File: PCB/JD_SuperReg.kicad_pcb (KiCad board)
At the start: 2 copper layers, 190.5 x 152.4 mm, 130 parts, among them J1 Conn_01x02_Male, J2 Conn_01x03_Male, J3 Conn_01x03_Male, J4 Conn_01x02_Male, Q101 D44H11, Q102 BC556, Q103 D45H11, Q104 BC546, Q201 D44H11, Q202 BC556, Q203 D45H11, Q204 BC546, T1 18V + 18V, T2 18V + 18V, U101 AD825ARZ, U102 AD825ARZ, U201 AD825ARZ, U202 AD825ARZ

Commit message: Finalized layout
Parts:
- removed C101, C102, C103, C104, C105, C106, C107, C108, C109, C110, C201, C202, C203, C204, C205, C206, C207, C208, C209, C210: 120uF, Capacitor_THT:CP_Radial_D10.0mm_P5.00mm
- removed C111, C112, C211, C212: 100pF, Capacitor_THT:C_Disc_D4.7mm_W2.5mm_P5.00mm
- removed C15, C16: 2200uF, Capacitor_THT:CP_Radial_D18.0mm_P7.50mm
- removed D101, D106, D201, D206: LED, LED_THT:LED_D3.0mm
- removed D102, D107, D202, D207: D_Zener, Diode_THT:D_DO-35_SOD27_P10.16mm_Horizontal
- removed D103, D104, D108, D109, D203, D204, D208, D209: D, Diode_THT:D_DO-35_SOD27_P10.16mm_Horizontal
- removed D105, D110, D205, D210: LM329, Package_TO_SOT_THT:TO-92_Inline
- removed F3, F4: Fuse, HP_Footprints:5x20mm-BK-1A3399-01-fuseholder
- removed HS101, HS102, HS201, HS202: Heatsink, Heatsink:Heatsink_Fischer_SK104-STCB_35x13mm__2xDrill3.5mm_ScrewM3
- removed Q101, Q201: D44H11, Package_TO_SOT_THT:TO-220-3_Vertical
- removed Q102, Q202: BC556, Package_TO_SOT_THT:TO-92_Inline
- removed Q103, Q203: D45H11, Package_TO_SOT_THT:TO-220-3_Vertical
- removed Q104, Q204: BC546, Package_TO_SOT_THT:TO-92_Inline
- removed R101, R108, R201, R208: 249R, Resistor_THT:R_Axial_DIN0207_L6.3mm_D2.5mm_P10.16mm_Horizontal
- removed R102, R109, R202, R209: 10K, Resistor_THT:R_Axial_DIN0207_L6.3mm_D2.5mm_P10.16mm_Horizontal
- removed R103, R110, R203, R210: 10R, Resistor_THT:R_Axial_DIN0207_L6.3mm_D2.5mm_P10.16mm_Horizontal
- removed R104, R111, R204, R211: 499R, Resistor_THT:R_Axial_DIN0207_L6.3mm_D2.5mm_P10.16mm_Horizontal
- removed R105, R112, R205, R212: 4.99K, Resistor_THT:R_Axial_DIN0207_L6.3mm_D2.5mm_P10.16mm_Horizontal
- removed R106, R107, R113, R114, R206, R207, R213, R214: 1K, Resistor_THT:R_Axial_DIN0207_L6.3mm_D2.5mm_P10.16mm_Horizontal
- removed R115, R116, R216: 100R, Resistor_THT:R_Axial_DIN0207_L6.3mm_D2.5mm_P10.16mm_Horizontal
- removed R215: 100, Resistor_THT:R_Axial_DIN0207_L6.3mm_D2.5mm_P10.16mm_Horizontal
- removed T1, T2: 18V + 18V, Super-Regulator Combined Dual:Talema-25VA-Transformer
- removed U101, U102, U201, U202: AD825ARZ, Package_SO:SOIC-8_3.9x4.9mm_P1.27mm
- added D10: 9V1, Diode_SMD:D_SOD-123, F.Cu at (105.9, 73.5)
- added D11: 4148, Diode_SMD:D_SOD-123, F.Cu at (113.4, 57.0)
- added D12: 4148, Diode_SMD:D_SOD-123, F.Cu at (113.4, 63.6)
- added D13: 4148, Diode_SMD:D_SOD-123, F.Cu at (113.4, 59.4)
- added D14: 4148, Diode_SMD:D_SOD-123, F.Cu at (113.4, 66.0)
- added D15: 9V1, Diode_SMD:D_SOD-123, F.Cu at (130.4, 56.2)
- added D16: 9V1, Diode_SMD:D_SOD-123, F.Cu at (132.8, 56.2)
- added D17: 9V1, Diode_SMD:D_SOD-123, F.Cu at (132.8, 66.8)
- added D18: 9V1, Diode_SMD:D_SOD-123, F.Cu at (130.4, 66.8)
- added D9: 9V1, Diode_SMD:D_SOD-123, F.Cu at (105.9, 49.6)
- added G***: LOGO, Ariamelon-Logo:Ariamelon_Logo_Medium_Mask, B.Cu at (143.6, 61.5)
- added H1: M3, Ariamelon-HolePad:MountingHole_3.2mm_M3_Pad, F.Cu at (59.0, 31.5)
- added H2: M3, Ariamelon-HolePad:MountingHole_3.2mm_M3_Pad, F.Cu at (59.0, 91.5)
- added H3: M3, Ariamelon-HolePad:MountingHole_3.2mm_M3_Pad, F.Cu at (149.0, 31.5)
- added H4: M3, Ariamelon-HolePad:MountingHole_3.2mm_M3_Pad, F.Cu at (149.0, 91.5)
- added HS1: Heatsink, Ariamelon-Misc:Heatsink, F.Cu at (117.5, 88.1)
- added HS2: Heatsink, Ariamelon-Misc:Heatsink, F.Cu at (117.5, 34.9)
- added J5: V-_Jumper, Ariamelon-Header:PinHeader_1x04_P2.54mm_Vertical_Jumper, F.Cu at (139.6, 72.9)
- added Q1: BCM857DS, Ariamelon-Package:SOT-23-6, F.Cu at (108.2, 44.5)
- added Q10: BCM847DS, Ariamelon-Package:SOT-23-6, F.Cu at (131.6, 73.4)
- added Q2: BCM847DS, Ariamelon-Package:SOT-23-6, F.Cu at (108.2, 78.5)
- added Q3: D44H11, Ariamelon-Package:TO-220-3_TO-247_Combined_Vertical, F.Cu at (117.5, 38.7)
- added Q4: D45H11, Ariamelon-Package:TO-220-3_TO-247_Combined_Vertical, F.Cu at (117.5, 84.3)
- added Q5: ZXTP2041F, Ariamelon-Package:SOT-23-3, F.Cu at (108.9, 50.4)
- added Q6: ZXTN2040F, Ariamelon-Package:SOT-23-3, F.Cu at (108.9, 72.6)
- added Q9: BCM857DS, Ariamelon-Package:SOT-23-6, F.Cu at (131.6, 49.6)
- added R11: 100, Resistor_SMD:R_MiniMELF_MMA-0204, F.Cu at (131.6, 52.6)
- added R12: 120, Resistor_SMD:R_MiniMELF_MMA-0204, F.Cu at (131.6, 70.4)
- added R13: 10K, Resistor_SMD:R_MiniMELF_MMA-0204, F.Cu at (135.4, 52.6)
- added R14: 10K, Resistor_SMD:R_MiniMELF_MMA-0204, F.Cu at (135.4, 70.4)
- added R15: 1k2, Resistor_SMD:R_MiniMELF_MMA-0204, F.Cu at (126.2, 48.8)
- added R16: 1k5, Resistor_SMD:R_MiniMELF_MMA-0204, F.Cu at (126.2, 56.4)
- added R17: 1k5, Resistor_SMD:R_MiniMELF_MMA-0204, F.Cu at (126.2, 66.6)
- added R18: 1k2, Resistor_SMD:R_MiniMELF_MMA-0204, F.Cu at (126.2, 74.2)
- added R5: 120, Resistor_SMD:R_MiniMELF_MMA-0204, F.Cu at (105.2, 44.4)
- added R6: 100, Resistor_SMD:R_MiniMELF_MMA-0204, F.Cu at (105.2, 78.5)
- added R7: 4k7, Resistor_SMD:R_MiniMELF_MMA-0204, F.Cu at (126.2, 52.6)
- added R8: 4k7, Resistor_SMD:R_MiniMELF_MMA-0204, F.Cu at (126.2, 70.4)
- added U1: ADA4522, Ariamelon-Package:SOIC-8_3.9x4.9mm_P1.27mm, F.Cu at (113.4, 52.0)
- added U2: ADA4522, Ariamelon-Package:SOIC-8_3.9x4.9mm_P1.27mm, F.Cu at (113.4, 71.0)
- C1: value 0.15uF -> 100n; footprint Capacitor_THT:C_Rect_L7.2mm_W3.5mm_P5.00mm_FKS2_FKP2_MKS2_MKP2 -> Ariamelon-Device:C_1206_3216Metric
- C10, C11: value 0.01uF -> 150u; footprint Capacitor_THT:C_Rect_L7.2mm_W2.5mm_P5.00mm_FKS2_FKP2_MKS2_MKP2 -> Capacitor_THT:CP_Radial_D8.0mm_P3.50mm
- C12, C13, C5, C7, C8: value 2200uF -> 150u; footprint Capacitor_THT:CP_Radial_D18.0mm_P7.50mm -> Capacitor_THT:CP_Radial_D8.0mm_P3.50mm
- C14, C6, C9: value 0.15uF -> 150u; footprint Capacitor_THT:C_Rect_L7.2mm_W3.5mm_P5.00mm_FKS2_FKP2_MKS2_MKP2 -> Capacitor_THT:CP_Radial_D8.0mm_P3.50mm
- C2: value 0.01uF -> 100n; footprint Capacitor_THT:C_Rect_L7.2mm_W2.5mm_P5.00mm_FKS2_FKP2_MKS2_MKP2 -> Ariamelon-Device:C_1206_3216Metric
- C3: value 0.01uF -> 4700u; footprint Capacitor_THT:C_Rect_L7.2mm_W2.5mm_P5.00mm_FKS2_FKP2_MKS2_MKP2 -> Capacitor_THT:CP_Radial_D18.0mm_P7.50mm
- C4: value 2200uF -> 4700u
- D1: value SB180 -> SBYV27; footprint Diode_THT:D_DO-41_SOD81_P10.16mm_Horizontal -> Diode_THT:D_DO-15_P10.16mm_Horizontal
- D2, D3, D4, D5, D6, D7, D8: value D -> SBYV27; footprint Diode_THT:D_DO-41_SOD81_P10.16mm_Horizontal -> Diode_THT:D_DO-15_P10.16mm_Horizontal
- F1, F2: value Fuse -> Fuse_Small; footprint HP_Footprints:5x20mm-BK-1A3399-01-fuseholder -> Fuse:Fuseholder_Cylinder-5x20mm_Schurter_0031_8201_Horizontal_Open
- J1: value Conn_01x02_Male -> V+_In; footprint HP_Footprints:2-pad-wire-connector-22-ga -> TerminalBlock_Phoenix:TerminalBlock_Phoenix_MKDS-1,5-2-5.08_1x02_P5.08mm_Horizontal
- J2: value Conn_01x03_Male -> V-_In; footprint HP_Footprints:3-pad-wire-connector-22-ga -> TerminalBlock_Phoenix:TerminalBlock_Phoenix_MKDS-1,5-2-5.08_1x02_P5.08mm_Horizontal
- J3: value Conn_01x03_Male -> Out; footprint HP_Footprints:3-pad-wire-connector-22-ga -> Ariamelon-Connector:TerminalBlock_Phoenix_MKDS-1,5-8-5.08_1x08_P5.08mm_Horizontal
- J4: value Conn_01x02_Male -> V+_Jumper; footprint HP_Footprints:2-pad-wire-connector-22-ga -> Ariamelon-Header:PinHeader_1x04_P2.54mm_Vertical_Jumper
- R1, R2: value 32R -> 10; footprint Resistor_THT:R_Axial_DIN0207_L6.3mm_D2.5mm_P10.16mm_Horizontal -> Resistor_SMD:R_MiniMELF_MMA-0204
- R3, R4: value 32R -> 10K; footprint Resistor_THT:R_Axial_DIN0207_L6.3mm_D2.5mm_P10.16mm_Horizontal -> Resistor_SMD:R_MiniMELF_MMA-0204
- moved J2 248.9 mm to (60.8, 69.1), turned to -90 degrees
- moved J3 186.1 mm to (147.2, 79.3)
- moved F1 168.3 mm to (64.5, 33.3), turned to 0 degrees
- moved F2 167.5 mm to (64.5, 89.7), turned to 0 degrees
- moved D6 164.1 mm to (70.9, 54.0), turned to 0 degrees
- moved D7 159.2 mm to (81.1, 69.0), turned to 180 degrees
- moved D5 157.7 mm to (70.9, 59.0), turned to 0 degrees
- moved D8 152.4 mm to (81.1, 64.0), turned to 180 degrees
- moved C13 152.3 mm to (120.5, 46.4)
- moved C11 148.7 mm to (120.5, 55.3), turned to -90 degrees
- moved R4 138.4 mm to (112.5, 77.6)
- moved C5 138.1 mm to (96.0, 36.3), turned to 180 degrees
- moved C14 137.4 mm to (120.5, 73.1), turned to -90 degrees
- moved R1 131.7 mm to (67.9, 53.7), turned to -90 degrees
- moved R2 129.1 mm to (67.9, 69.3), turned to 90 degrees
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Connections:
- C1 pad 1: Net-(C1-Pad1) -> Net-(D1-A)
- C10 pad 1: Net-(C10-Pad1) -> GND
- C10 pad 2: /Raw Power/V2-COM -> VEE
- C11 pad 1: /Raw Power/V2-COM -> Net-(D11-A)
- C11 pad 2: Net-(C11-Pad2) -> Net-(D16-A)
- C12 pad 1: Net-(C12-Pad1) -> Net-(D17-A)
- C12 pad 2: /Raw Power/V2-COM -> Net-(D12-A)
- C13 pad 1: /Regulator 2/V2-IN-POS -> Net-(J3-Pin_7)
- C13 pad 2: /Raw Power/V2-COM -> Net-(D11-K)
- C14 pad 1: Net-(C14-Pad1) -> Net-(D12-K)
- C14 pad 2: Net-(C11-Pad2) -> Net-(J3-Pin_2)
- C2 pad 1: Net-(C1-Pad1) -> Net-(D4-K)
- C2 pad 2: /Raw Power/V1-COM -> Net-(C2-Pad2)
- C3 pad 1: /Raw Power/V1-COM -> Net-(Q1B-E2)
- C3 pad 2: Net-(C3-Pad2) -> GND
- C4 pad 1: Net-(C4-Pad1) -> GND
- C4 pad 2: /Raw Power/V1-COM -> Net-(Q2B-E2)
- C5 pad 1: /Regulator 1/V1-IN-POS -> Net-(Q1B-E2)
- C5 pad 2: /Raw Power/V1-COM -> GND
- C6 pad 1: Net-(C6-Pad1) -> GND
- C6 pad 2: Net-(C3-Pad2) -> Net-(Q2B-E2)
- C7 pad 1: /Raw Power/V1-COM -> Net-(D9-K)
- C7 pad 2: Net-(C7-Pad2) -> Net-(D9-A)
- C8 pad 1: /Raw Power/V1-COM -> Net-(D10-K)
- C8 pad 2: /Regulator 1/V1-IN-NEG -> Net-(D10-A)
- C9 pad 1: Net-(C10-Pad1) -> VCC
- C9 pad 2: Net-(C9-Pad2) -> GND
- D1 pad 1: Net-(C1-Pad1) -> Net-(D1-K)
- D1 pad 2: Net-(C7-Pad2) -> Net-(D1-A)
- D2 pad 1: Net-(C4-Pad1) -> Net-(D1-K)
- D2 pad 2: Net-(C1-Pad1) -> Net-(D2-A)
- D3 pad 1: Net-(C3-Pad2) -> Net-(D3-K)
- D3 pad 2: Net-(C7-Pad2) -> Net-(D3-A)
- D4 pad 1: Net-(C4-Pad1) -> Net-(D4-K)
- D4 pad 2: Net-(C3-Pad2) -> Net-(D3-A)
- D5 pad 1: Net-(C10-Pad1) -> Net-(D1-A)
- D5 pad 2: Net-(C15-Pad2) -> GND
- D6 pad 1: Net-(C12-Pad1) -> Net-(D2-A)
- D6 pad 2: Net-(C10-Pad1) -> GND
- D7 pad 1: Net-(C11-Pad2) -> GND
- D7 pad 2: Net-(C15-Pad2) -> Net-(D3-K)
- D8 pad 1: Net-(C12-Pad1) -> GND
- D8 pad 2: Net-(C11-Pad2) -> Net-(D4-K)
- F1 pad 1: /Regulator 1/V1-IN-POS -> Net-(D1-K)
- F1 pad 2: Net-(C4-Pad1) -> Net-(Q1B-E2)
- F2 pad 1: /Regulator 1/V1-IN-NEG -> Net-(D3-A)
- F2 pad 2: Net-(C7-Pad2) -> Net-(Q2B-E2)
- J1 pad 1: /Raw Power/AC1 -> Net-(D1-A)
- J1 pad 2: /Raw Power/AC2 -> Net-(D2-A)
- J2 pad 1: /Regulator 1/V1-OUT-NEG -> Net-(D3-K)
- J2 pad 2: /Raw Power/V1-COM -> Net-(D4-K)
- J3 pad 1: /Regulator 2/V2-OUT-NEG -> VEE
- J3 pad 2: /Raw Power/V2-COM -> Net-(J3-Pin_2)
- J3 pad 3: /Regulator 2/V2-OUT-POS -> Net-(D17-A)
- J4 pad 1: /Raw Power/AC1 -> VCC
- J4 pad 2: /Raw Power/SW2 -> Net-(J3-Pin_7)
- R1 pad 2: /Raw Power/V1-COM -> Net-(D2-A)
- R2 pad 1: /Raw Power/V1-COM -> Net-(C2-Pad2)
- R2 pad 2: Net-(C6-Pad1) -> Net-(D3-K)
- R3 pad 1: Net-(C9-Pad2) -> Net-(Q1A-B1)
- R3 pad 2: /Raw Power/V2-COM -> GND
- R4 pad 1: /Raw Power/V2-COM -> Net-(Q2A-B1)
- R4 pad 2: Net-(C14-Pad1) -> GND
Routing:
- net /Raw Power/V2-COM: track 379.6 -> 0.00 mm
- net /Raw Power/V1-COM: track 379.4 -> 0.00 mm
- net /Raw Power/AC2: track 152.1 -> 0.00 mm
- net /Raw Power/SW2: track 149.6 -> 0.00 mm
- net /Regulator 1/V1-OUT-POS: track 119.3 -> 0.00 mm, vias 1 -> 0
- net /Regulator 2/V2-OUT-POS: track 118.3 -> 0.00 mm, vias 1 -> 0
- net /Regulator 1/V1-OUT-NEG: track 91.9 -> 0.00 mm, vias 1 -> 0
- net /Regulator 2/V2-OUT-NEG: track 91.9 -> 0.00 mm, vias 1 -> 0
- net /Regulator 1/V1-IN-POS: track 86.5 -> 0.00 mm
- net /Regulator 2/V2-IN-POS: track 86.4 -> 0.00 mm
- net /Regulator 2/V2-IN-NEG: track 85.7 -> 0.00 mm
- net /Regulator 1/V1-IN-NEG: track 85.7 -> 0.00 mm
- net Net-(C207-Pad1): track 56.5 -> 0.00 mm
- net Net-(C107-Pad1): track 56.5 -> 0.00 mm
- net Net-(C203-Pad2): track 49.1 -> 0.00 mm
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- added copper zone on B.Cu, net GND
- added copper zone on F.Cu, net GND
- added copper zone on F.Cu, net Net-(C1-Pad2)
- added copper zone on F.Cu, net Net-(C2-Pad2)
- added copper zone on B.Cu, net Net-(D1-A)
- added copper zone on F.Cu, net Net-(D1-A)
- added copper zone on F.Cu, net Net-(D1-K)
- added copper zone on B.Cu, net Net-(D2-A)
- added copper zone on F.Cu, net Net-(D2-A)
- added copper zone on F.Cu, net Net-(D3-A)
- added copper zone on B.Cu, net Net-(D3-K)
- added copper zone on F.Cu, net Net-(D3-K)
- added copper zone on B.Cu, net Net-(D4-K)
- added copper zone on F.Cu, net Net-(D4-K)
- added copper zone on F.Cu, net Net-(Q1B-E2)
- added copper zone on F.Cu, net Net-(Q2B-E2)
- added copper zone on B.Cu, net VCC
- added copper zone on B.Cu, net VEE
- removed copper zone on F.Cu, net /Raw Power/V1-COM
- removed copper zone on F.Cu, net /Raw Power/V2-COM
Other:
- board size 190.5 x 152.4 mm -> 97 x 67 mm
- rule pad_to_mask_clearance: 0.051 -> 0
- board text added: "Jung/Didden Super Regulator V1.0"
- board text removed: "AC"
- board text removed: "COM"
- board text removed: "NEG"
- board text removed: "POS"
- board text removed: "SW"

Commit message: Initial public upload
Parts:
- added C15: 100p, Ariamelon-Device:C_0805_2012Metric, F.Cu at (134.1, 47.8)
- added C16: 100p, Ariamelon-Device:C_0805_2012Metric, F.Cu at (134.1, 75.2)
- added J6: V-_Sen+_Jumper, Ariamelon-Header:PinHeader_1x02_P2.54mm_Vertical_Jumper, F.Cu at (139.6, 66.6)
- added J7: V-_Sen-_Jumper, Ariamelon-Header:PinHeader_1x02_P2.54mm_Vertical_Jumper, F.Cu at (139.6, 74.2)
- added R10: 120, Resistor_SMD:R_MiniMELF_MMA-0204, F.Cu at (134.7, 77.4)
- added R9: 120, Resistor_SMD:R_MiniMELF_MMA-0204, F.Cu at (134.7, 45.6)
- added RV1: 1k, Potentiometer_THT:Potentiometer_Bourns_3266W_Vertical, F.Cu at (124.3, 50.1)
- added RV2: 1k, Potentiometer_THT:Potentiometer_Bourns_3266W_Vertical, F.Cu at (126.8, 72.9)
- G***: footprint Ariamelon-Logo:Ariamelon_Logo_Medium_Mask -> Ariamelon-Logo:Ariamelon_Logo_Small_CU
- J4: value V+_Jumper -> V+_Sen+_Jumper; footprint Ariamelon-Header:PinHeader_1x04_P2.54mm_Vertical_Jumper -> Ariamelon-Header:PinHeader_1x02_P2.54mm_Vertical_Jumper
- J5: value V-_Jumper -> V+_Sen-_Jumper; footprint Ariamelon-Header:PinHeader_1x04_P2.54mm_Vertical_Jumper -> Ariamelon-Header:PinHeader_1x02_P2.54mm_Vertical_Jumper
- Q3: value D44H11 -> BDW93C
- Q4: value D45H11 -> BDW94C
- Q5: value ZXTP2041F -> MMBT5087
- Q6: value ZXTN2040F -> MMBT5089
- R11, R6: value 100 -> 120
- R15, R18: value 1k2 -> 560
- R16, R17: value 1k5 -> 560
- R7, R8: value 4k7 -> 10K
- moved G*** 82.6 mm to (61.0, 61.5), turned to -90 degrees
- moved J5 19.1 mm to (139.6, 53.9)
- moved R8 6.61 mm to (130.8, 65.6), turned to -90 degrees
- moved R7 6.61 mm to (130.8, 57.4), turned to -90 degrees
- moved C11 3.96 mm to (118.7, 58.8), turned to 90 degrees
- moved C12 3.96 mm to (118.7, 67.7), turned to 90 degrees
- moved J4 3.81 mm to (139.6, 46.3)
- moved D17 3.00 mm to (135.6, 65.6)
- moved D18 3.00 mm to (133.2, 65.6)
- moved D15 3.00 mm to (133.2, 57.4)
- moved D16 3.00 mm to (135.6, 57.4)
- moved D10 2.06 mm to (104.0, 72.6)
- moved D9 2.02 mm to (104.0, 50.4)
- moved D11 1.86 mm to (111.5, 57.2)
- moved D12 1.86 mm to (111.5, 63.4)
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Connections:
- C13 pad 1: Net-(J3-Pin_7) -> Net-(Q9B-E2)
- C14 pad 2: Net-(J3-Pin_2) -> Net-(Q10B-E2)
- J5 pad 1: GND -> Net-(D16-A)
- J5 pad 2: Net-(D17-A) -> GND
- Q10 pad 4: Net-(J3-Pin_2) -> Net-(Q10B-E2)
- Q9 pad 4: Net-(J3-Pin_7) -> Net-(Q9B-E2)
- R11 pad 1: Net-(J3-Pin_7) -> Net-(Q9B-E2)
- R12 pad 2: Net-(J3-Pin_2) -> Net-(Q10B-E2)
- R15 pad 1: Net-(J3-Pin_7) -> Net-(Q9B-E2)
- R15 pad 2: Net-(D11-K) -> Net-(R15-Pad2)
- R16 pad 1: Net-(D11-K) -> Net-(R16-Pad1)
- R17 pad 2: Net-(D12-K) -> Net-(R17-Pad2)
- R18 pad 1: Net-(D12-K) -> Net-(R18-Pad1)
- R18 pad 2: Net-(J3-Pin_2) -> Net-(Q10B-E2)
- R7 pad 1: Net-(D11-A) -> Net-(D15-A)
- R7 pad 2: Net-(D15-A) -> Net-(D11-A)
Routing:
- net Net-(Q10B-E2): track 0.00 -> 32.0 mm
- net Net-(J3-Pin_2): track 39.3 -> 12.1 mm
- net Net-(Q9B-E2): track 0.00 -> 24.6 mm
- net Net-(J3-Pin_7): track 34.5 -> 12.1 mm
- net Net-(D16-A): track 30.2 -> 41.2 mm
- net Net-(D17-A): track 30.8 -> 41.6 mm
- net Net-(D12-A): track 19.7 -> 27.3 mm
- net Net-(D9-K): track 39.8 -> 32.3 mm
- net Net-(D11-A): track 16.8 -> 23.4 mm
- net Net-(R18-Pad1): track 0.00 -> 4.55 mm
- net Net-(R17-Pad2): track 0.00 -> 4.53 mm
- net Net-(D18-A): track 9.14 -> 12.4 mm
- net Net-(D12-K): track 24.3 -> 21.7 mm
- net Net-(R16-Pad1): track 0.00 -> 2.09 mm
- net Net-(R15-Pad2): track 0.00 -> 1.98 mm
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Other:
- board text added: "AC+"
- board text added: "AC-"
- board text added: "GND"
- board text added: "Sen+"
- board text added: "Sen-"
- board text added: "V+"
- board text added: "V+ Sense Jumpers"
- board text added: "V-"
- board text added: "V- Sense Jumpers"

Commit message: 27/09/2023 update
Changed board to 4 layers. Removed fuses. Added MOV surge protection and resistors for RC input filter.
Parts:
- removed the D3 at (70.9, 79.0)
- removed the D4 at (70.9, 74.0)
- removed the D5 at (70.9, 59.0)
- removed the D6 at (70.9, 54.0)
- removed the D7 at (81.1, 69.0)
- removed the D8 at (81.1, 64.0)
- removed F1, F2: Fuse_Small, Fuse:Fuseholder_Cylinder-5x20mm_Schurter_0031_8201_Horizontal_Open
- removed the J3 at (147.2, 79.3)
- added R3: 4R7, Resistor_THT:R_Axial_DIN0617_L17.0mm_D6.0mm_P20.32mm_Horizontal, F.Cu at (65.0, 38.3)
- added R4: 4R7, Resistor_THT:R_Axial_DIN0617_L17.0mm_D6.0mm_P20.32mm_Horizontal, F.Cu at (65.0, 84.7)
- added R5: 4R7, Resistor_THT:R_Axial_DIN0617_L17.0mm_D6.0mm_P20.32mm_Horizontal, F.Cu at (65.0, 31.5)
- added R6: 4R7, Resistor_THT:R_Axial_DIN0617_L17.0mm_D6.0mm_P20.32mm_Horizontal, F.Cu at (65.0, 91.5)
- added TH1: 40VAC, Varistor:RV_Disc_D9mm_W5.2mm_P5mm, F.Cu at (68.9, 52.0)
- added TH2: 40VAC, Varistor:RV_Disc_D9mm_W5.2mm_P5mm, F.Cu at (68.9, 68.5)
- D1, D2: value SBYV27 -> 4A; footprint Diode_THT:D_DO-15_P10.16mm_Horizontal -> Diode_THT:Diode_Bridge_Vishay_GBU
- G***: footprint Ariamelon-Logo:Ariamelon_Logo_Small_CU -> Ariamelon-Logo:Ariamelon_Logo_Small_Mask
- J1: value V+_In -> In; footprint TerminalBlock_Phoenix:TerminalBlock_Phoenix_MKDS-1,5-2-5.08_1x02_P5.08mm_Horizontal -> TerminalBlock_Phoenix:TerminalBlock_Phoenix_MKDS-1,5-4-5.08_1x04_P5.08mm_Horizontal
- J2: value V-_In -> Out; footprint TerminalBlock_Phoenix:TerminalBlock_Phoenix_MKDS-1,5-2-5.08_1x02_P5.08mm_Horizontal -> Ariamelon-Connector:TerminalBlock_Phoenix_MKDS-1,5-8-5.08_1x08_P5.08mm_Horizontal
- J3: renamed from J4; value V+_Sen+_Jumper -> V+_Sen+
- J4: renamed from J5; value V+_Sen-_Jumper -> V+_Sen-
- J5: renamed from J6; value V-_Sen+_Jumper -> V-_Sen+
- J6: renamed from J7; value V-_Sen-_Jumper -> V-_Sen-
- moved J2 87.0 mm to (147.2, 79.3), turned to 90 degrees
- moved G*** 82.9 mm to (143.9, 61.5), turned to 90 degrees
- moved D2 34.4 mm to (78.6, 78.3)
- moved D1 18.2 mm to (63.4, 44.8), turned to 0 degrees
- moved R1 6.95 mm to (73.2, 49.2), turned to 0 degrees
- moved R2 6.95 mm to (73.2, 73.8), turned to 0 degrees
- moved J1 5.08 mm to (60.8, 53.9)
- moved C4 1.00 mm to (91.0, 67.4)
- moved C3 0.98 mm to (91.0, 48.1)
- moved C1 0.58 mm to (68.4, 49.2), turned to 0 degrees
- moved C2 0.58 mm to (68.4, 73.8), turned to 0 degrees
- moved Q1 0.05 mm to (106.4, 44.6)
- moved Q2 0.05 mm to (106.4, 78.4)
- moved R10 0.05 mm to (103.4, 78.4)
- moved R7 0.05 mm to (110.7, 45.5)
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- renumbered D16 to D10, D17 to D11, D18 to D12, D9 to D3, D10 to D4, D11 to D5, D12 to D6, D13 to D7, D14 to D8, D15 to D9, Q9 to Q7, Q10 to Q8, R6 to R10, R7 to R11, R8 to R12, R11 to R13, R12 to R14, R13 to R15, R14 to R16, R15 to R17, R16 to R18, R17 to R19, R18 to R20, R9 to R21, R10 to R22, R3 to R7, R4 to R8, R5 to R9
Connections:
- C11 pad 2: Net-(D16-A) -> Net-(D10-A)
- C12 pad 1: Net-(D17-A) -> Net-(D11-A)
- C15 pad 2: Net-(D16-A) -> Net-(D10-A)
- C16 pad 2: Net-(D17-A) -> Net-(D11-A)
- C2 pad 1: Net-(D4-K) (its old number) -> Net-(J1-Pin_4)
- D1 pad 1: Net-(D1-K) -> Net-(D1-+)
- D10 pad 2: Net-(D16-A) -> Net-(D10-A)
- D11 pad 2: Net-(D17-A) -> Net-(D11-A)
- D2 pad 1: Net-(D1-K) -> GND
- D2 pad 2: Net-(D2-A) -> Net-(J1-Pin_3)
- J1 pad 2: Net-(D2-A) -> Net-(J1-Pin_2)
- J2 pad 1: Net-(D3-K) (its old number) -> VEE
- J2 pad 2: Net-(D4-K) (its old number) -> Net-(J2-Pin_2)
- J3 pad 2: Net-(J3-Pin_7) -> Net-(J2-Pin_7)
- J4 pad 1: Net-(D16-A) -> Net-(D10-A)
- J5 pad 2: Net-(D17-A) -> Net-(D11-A)
- J6 pad 1: Net-(J3-Pin_2) -> Net-(J2-Pin_2)
- R1 pad 2: Net-(D2-A) -> Net-(J1-Pin_2)
- R15 pad 2: Net-(D16-A) -> Net-(D10-A)
- R16 pad 1: Net-(D17-A) -> Net-(D11-A)
- R18 pad 2: Net-(D16-A) -> Net-(D10-A)
- R19 pad 1: Net-(D17-A) -> Net-(D11-A)
- R2 pad 2: Net-(D3-K) (its old number) -> Net-(J1-Pin_3)
- R21 pad 2: Net-(J3-Pin_7) -> Net-(J2-Pin_7)
- R22 pad 2: Net-(J3-Pin_2) -> Net-(J2-Pin_2)
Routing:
- net Net-(D11-A): track 0.00 -> 41.7 mm
- net Net-(D17-A): track 41.6 -> 0.00 mm
- net Net-(D10-A): track 0.00 -> 41.2 mm
- net Net-(D16-A): track 41.2 -> 0.00 mm
- net Net-(J3-Pin_2): track 12.1 -> 0.00 mm
- net Net-(J2-Pin_2): track 0.00 -> 12.1 mm
- net Net-(J3-Pin_7): track 12.1 -> 0.00 mm
- net Net-(J2-Pin_7): track 0.00 -> 12.1 mm
- net GND: vias 322 -> 344
- added copper zone on In1.Cu, net GND
- added copper zone on In2.Cu, net GND
- added copper zone on B.Cu, net Net-(D1-+)
- added copper zone on F.Cu, net Net-(D1-+)
- added copper zone on In1.Cu, net Net-(D1-+)
- added copper zone on In2.Cu, net Net-(D1-+)
- added copper zone on B.Cu, net Net-(D2--)
- added copper zone on F.Cu, net Net-(D2--)
- added copper zone on In1.Cu, net Net-(D2--)
- added copper zone on In2.Cu, net Net-(D2--)
- added copper zone on In1.Cu, net Net-(J1-Pin_1)
- added copper zone on In2.Cu, net Net-(J1-Pin_1)
- added copper zone on B.Cu, net Net-(J1-Pin_2)
- added copper zone on F.Cu, net Net-(J1-Pin_2)
- added copper zone on In1.Cu, net Net-(J1-Pin_2)
- added copper zone on In2.Cu, net Net-(J1-Pin_2)
- added copper zone on B.Cu, net Net-(J1-Pin_3)
- added copper zone on F.Cu, net Net-(J1-Pin_3)
- added copper zone on In1.Cu, net Net-(J1-Pin_3)
- added copper zone on In2.Cu, net Net-(J1-Pin_3)
- added copper zone on B.Cu, net Net-(J1-Pin_4)
- added copper zone on F.Cu, net Net-(J1-Pin_4)
- added copper zone on In1.Cu, net Net-(J1-Pin_4)
- added copper zone on In2.Cu, net Net-(J1-Pin_4)
- added copper zone on In1.Cu, net Net-(Q1B-E2)
- added copper zone on In1.Cu, net Net-(Q2B-E2)
- added copper zone on In2.Cu, net VCC
- added copper zone on In2.Cu, net VEE
- removed copper zone on F.Cu, net Net-(D1-K)
- removed copper zone on B.Cu, net Net-(D2-A)
- removed copper zone on F.Cu, net Net-(D2-A)
- removed copper zone on F.Cu, net Net-(D3-A) (its old number)
- removed copper zone on B.Cu, net Net-(D3-K) (its old number)
- removed copper zone on F.Cu, net Net-(D3-K) (its old number)
- removed copper zone on B.Cu, net Net-(D4-K) (its old number)
- removed copper zone on F.Cu, net Net-(D4-K) (its old number)
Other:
- copper layers 2 -> 4

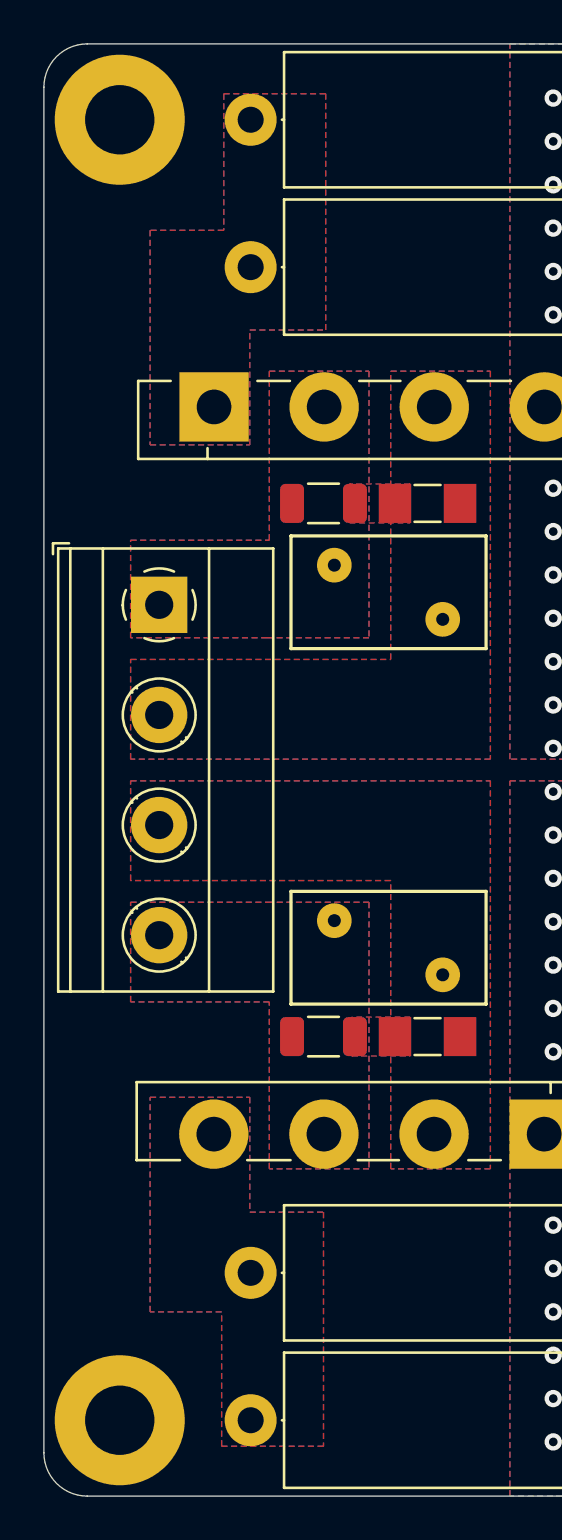
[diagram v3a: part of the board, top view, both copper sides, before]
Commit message: 05/10/2023 update
Changed output voltage to 15V.
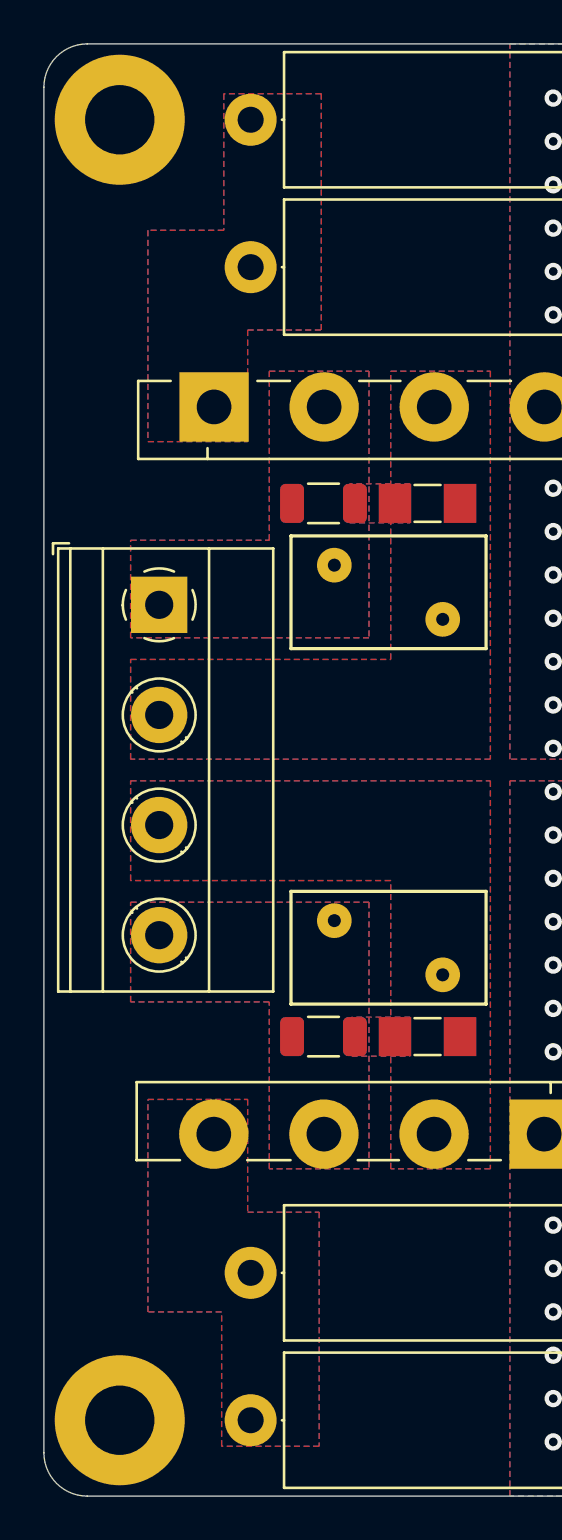
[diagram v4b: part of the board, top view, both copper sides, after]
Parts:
- C10, C11, C12, C13, C14, C5, C6, C7, C8, C9: value 150u -> 220u
- D10, D11, D12, D3, D4, D9: value 9V1 -> 7V5
- U1, U2: value ADA4522 -> ADA4610-1
